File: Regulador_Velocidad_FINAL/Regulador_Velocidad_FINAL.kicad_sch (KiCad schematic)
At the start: 5 parts

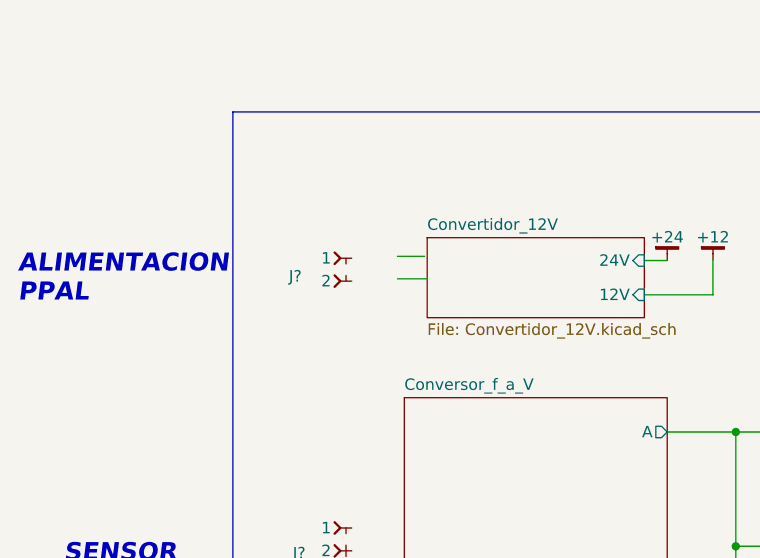
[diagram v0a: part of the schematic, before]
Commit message: Monitor_speed: Changes Schematics
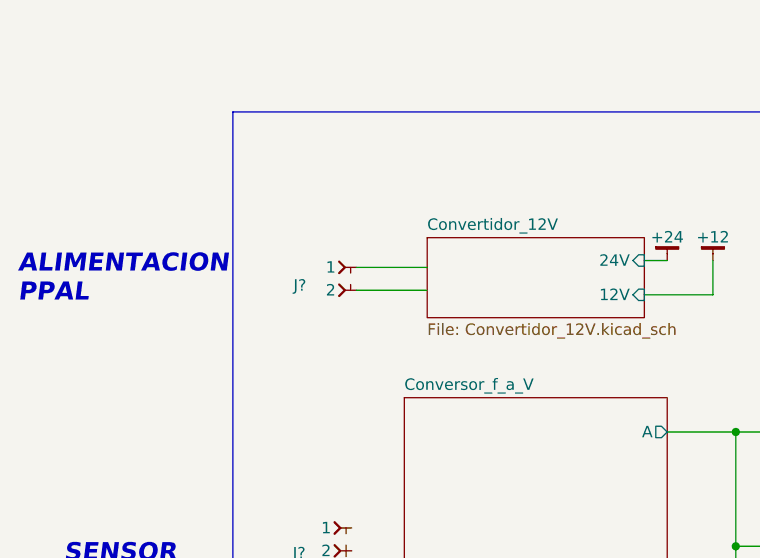
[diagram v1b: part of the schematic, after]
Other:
- moved on the sheet: J?
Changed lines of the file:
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@@
 (kicad_sch (version 20210621) (generator eeschema)
   (paper "A4")
+  (junction (at 149.098 100.33) (diameter 0) (color 0 0 0 0))
   (junction (at 149.098 113.03) (diameter 0) (color 0 0 0 0))
-  (junction (at 149.098 100.33) (diameter 0) (color 0 0 0 0))
   (wire (pts (xy 149.098 128.27) (xy 149.098 113.03))
     (stroke (width 0) (type default) (color 0 0 0 0))
   )
-  (wire (pts (xy 111.506 83.312) (xy 114.808 83.312))
-    (stroke (width 0) (type default) (color 0 0 0 0))
-  )
-  (wire (pts (xy 111.508 80.81) (xy 114.508 80.81))
+  (wire (pts (xy 106.934 84.582) (xy 114.808 84.582))
     (stroke (width 0) (type default) (color 0 0 0 0))
   )
@@
     (stroke (width 0) (type default) (color 0 0 0 0))
   )
+  (wire (pts (xy 146.558 85.09) (xy 146.558 81.28))
+    (stroke (width 0) (type default) (color 0 0 0 0))
+  )
   (wire (pts (xy 138.938 85.09) (xy 146.558 85.09))
     (stroke (width 0) (type default) (color 0 0 0 0))
   )
-  (wire (pts (xy 146.558 85.09) (xy 146.558 81.28))
+  (wire (pts (xy 106.934 82.042) (xy 114.808 82.042))
     (stroke (width 0) (type default) (color 0 0 0 0))
   )
@@
     (stroke (width 0) (type default) (color 0 0 0 0))
   )
+  (polyline (pts (xy 93.218 64.77) (xy 93.218 146.05))
+    (stroke (width 0) (type default) (color 0 0 0 0))
+  )
   (polyline (pts (xy 93.218 64.77) (xy 210.058 64.77))
     (stroke (width 0) (type default) (color 0 0 0 0))
   )
   (polyline (pts (xy 210.058 146.05) (xy 93.218 146.05))
-    (stroke (width 0) (type default) (color 0 0 0 0))
-  )
-  (polyline (pts (xy 93.218 64.77) (xy 93.218 146.05))
     (stroke (width 0) (type default) (color 0 0 0 0))
   )
@@
     (pin "3")
   )
-  (symbol (lib_id "conn-100mil:CONN-100MIL-F-1x2") (at 105.156 81.026 0) (mirror y) (unit 1)
-    (in_bom yes) (on_board yes)
-    (property "Reference" "J?" (id 0) (at 100.156 83.026 0))
-    (property "Value" "CONN-100MIL-F-1x2" (id 1) (at 105.0925 79.1996 0)
-      (effects (font (size 1.27 1.27)) hide)
-    )
-    (property "Footprint" "conn-100mil:CONN-100MIL-F-1x2" (id 2) (at 105.156 81.026 0)
-      (effects (font (size 1.27 1.27)) hide)
-    )
-    (property "Datasheet" "" (id 3) (at 105.156 81.026 0))
+  (symbol (lib_id "conn-100mil:CONN-100MIL-F-1x2") (at 105.664 82.042 0) (mirror y) (unit 1)
+    (in_bom yes) (on_board yes)
+    (property "Reference" "J?" (id 0) (at 100.664 84.042 0))
+    (property "Value" "CONN-100MIL-F-1x2" (id 1) (at 105.6005 80.2156 0)
+      (effects (font (size 1.27 1.27)) hide)
+    )
+    (property "Footprint" "conn-100mil:CONN-100MIL-F-1x2" (id 2) (at 105.664 82.042 0)
+      (effects (font (size 1.27 1.27)) hide)
+    )
+    (property "Datasheet" "" (id 3) (at 105.664 82.042 0))
     (pin "1")
     (pin "2")
@@
       (reference "#PWR?") (unit 1) (value "+24") (footprint "")
     )
+    (path "/00000000-0000-0000-0000-0000612e15a4/1888b6cc-01b4-4d63-b759-ff08c40e2ea5"
+      (reference "#PWR?") (unit 1) (value "+12") (footprint "")
+    )
     (path "/00000000-0000-0000-0000-0000612e15a4/191b58eb-f343-4e44-963c-006bd7e58632"
       (reference "#PWR?") (unit 1) (value "+12") (footprint "")
@@
       (reference "#PWR?") (unit 1) (value "GND") (footprint "")
     )
+    (path "/00000000-0000-0000-0000-0000612e15a4/bf605f14-3222-4811-bade-070d22a5da3e"
+      (reference "#PWR?") (unit 1) (value "+12") (footprint "")
+    )
     (path "/00000000-0000-0000-0000-0000612e3fd7/d6147ff6-8513-43f1-9dd7-b83e35a8992b"

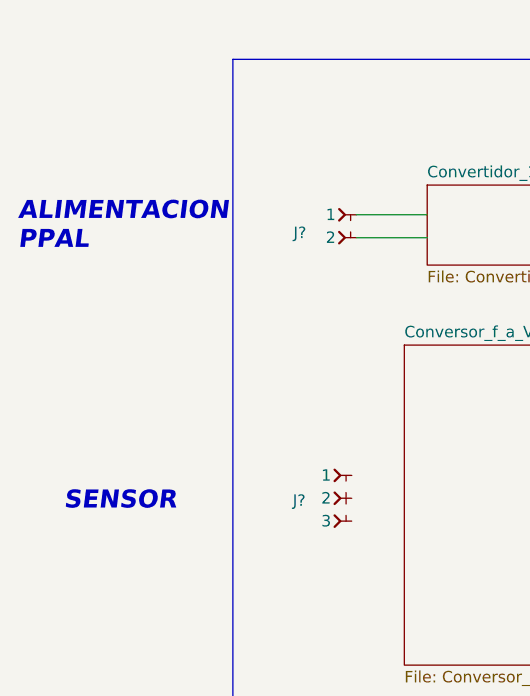
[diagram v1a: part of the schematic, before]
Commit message: Speed_Monitor: Changes on schematics
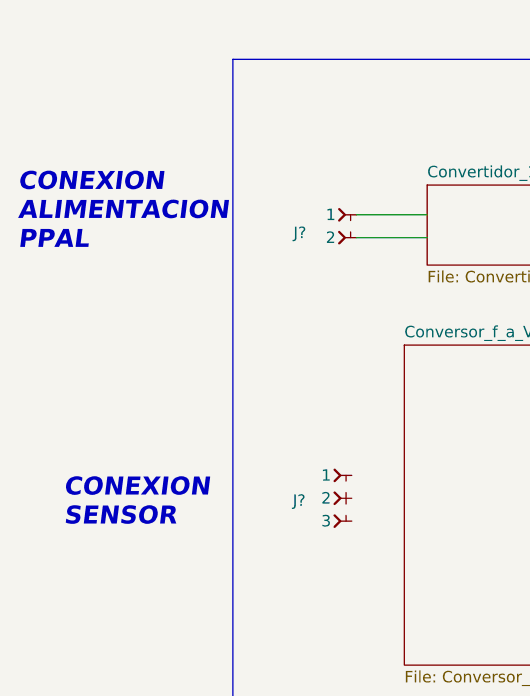
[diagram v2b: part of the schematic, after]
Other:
- note added: "CONEXION ALIMENTACION PPAL"
- note added: "CONEXION SENSOR"
- note removed: "ALIMENTACION PPAL"
- note removed: "SENSOR"
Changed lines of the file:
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@@
 (kicad_sch (version 20210621) (generator eeschema)
   (paper "A4")
+  (junction (at 149.098 113.03) (diameter 0) (color 0 0 0 0))
   (junction (at 149.098 100.33) (diameter 0) (color 0 0 0 0))
-  (junction (at 149.098 113.03) (diameter 0) (color 0 0 0 0))
   (wire (pts (xy 149.098 128.27) (xy 149.098 113.03))
     (stroke (width 0) (type default) (color 0 0 0 0))
@@
     (stroke (width 0) (type default) (color 0 0 0 0))
   )
+  (wire (pts (xy 138.938 85.09) (xy 146.558 85.09))
+    (stroke (width 0) (type default) (color 0 0 0 0))
+  )
   (wire (pts (xy 146.558 85.09) (xy 146.558 81.28))
     (stroke (width 0) (type default) (color 0 0 0 0))
   )
-  (wire (pts (xy 138.938 85.09) (xy 146.558 85.09))
-    (stroke (width 0) (type default) (color 0 0 0 0))
-  )
   (wire (pts (xy 106.934 82.042) (xy 114.808 82.042))
     (stroke (width 0) (type default) (color 0 0 0 0))
@@
     (stroke (width 0) (type default) (color 0 0 0 0))
   )
+  (polyline (pts (xy 210.058 146.05) (xy 93.218 146.05))
+    (stroke (width 0) (type default) (color 0 0 0 0))
+  )
+  (polyline (pts (xy 93.218 64.77) (xy 210.058 64.77))
+    (stroke (width 0) (type default) (color 0 0 0 0))
+  )
+  (polyline (pts (xy 210.058 64.77) (xy 210.058 146.05))
+    (stroke (width 0) (type default) (color 0 0 0 0))
+  )
   (polyline (pts (xy 93.218 64.77) (xy 93.218 146.05))
     (stroke (width 0) (type default) (color 0 0 0 0))
   )
-  (polyline (pts (xy 93.218 64.77) (xy 210.058 64.77))
-    (stroke (width 0) (type default) (color 0 0 0 0))
-  )
-  (polyline (pts (xy 210.058 146.05) (xy 93.218 146.05))
-    (stroke (width 0) (type default) (color 0 0 0 0))
-  )
-  (polyline (pts (xy 210.058 64.77) (xy 210.058 146.05))
-    (stroke (width 0) (type default) (color 0 0 0 0))
-  )
   (wire (pts (xy 138.938 81.28) (xy 141.478 81.28))
     (stroke (width 0) (type default) (color 0 0 0 0))
@@
     (effects (font (size 2 2) (thickness 0.4) bold italic) (justify left bottom))
   )
-  (text "SENSOR" (at 74.422 115.062 0)
-    (effects (font (size 2 2) (thickness 0.4) bold italic) (justify left bottom))
-  )
-  (text "ALIMENTACION\nPPAL" (at 69.342 86.106 0)
+  (text "CONEXION\nSENSOR" (at 74.422 116.84 0)
+    (effects (font (size 2 2) (thickness 0.4) bold italic) (justify left bottom))
+  )
+  (text "CONEXION\nALIMENTACION\nPPAL" (at 69.342 86.106 0)
     (effects (font (size 2 2) (thickness 0.4) bold italic) (justify left bottom))
   )
@@
       (reference "#PWR0105") (unit 1) (value "GND") (footprint "")
     )
-    (path "/00000000-0000-0000-0000-0000612e15a4/00000000-0000-0000-0000-00006131281b"
-      (reference "#PWR0106") (unit 1) (value "GND") (footprint "")
-    )
     (path "/00000000-0000-0000-0000-0000612e15a4/00000000-0000-0000-0000-000061312847"
       (reference "#PWR0107") (unit 1) (value "GND") (footprint "")
     )
-    (path "/00000000-0000-0000-0000-0000612e15a4/00000000-0000-0000-0000-000061312853"
-      (reference "#PWR0108") (unit 1) (value "GND") (footprint "")
-    )
     (path "/00000000-0000-0000-0000-0000612e15a4/00000000-0000-0000-0000-000061312865"
       (reference "#PWR0109") (unit 1) (value "GND") (footprint "")
@@
       (reference "#PWR?") (unit 1) (value "+12") (footprint "")
     )
+    (path "/00000000-0000-0000-0000-0000612e15a4/30ff6dd4-1562-413a-81cf-b765833a91db"
+      (reference "#PWR?") (unit 1) (value "+12") (footprint "")
+    )
     (path "/00000000-0000-0000-0000-000061322896/8bb79843-2e88-4533-bc74-6205b95b5360"
       (reference "#PWR?") (unit 1) (value "+24") (footprint "")
@@
       (reference "#PWR?") (unit 1) (value "GND") (footprint "")
     )
+    (path "/00000000-0000-0000-0000-0000612e15a4/b823652e-3346-4fc3-9ee0-0de81291789f"
+      (reference "#PWR?") (unit 1) (value "GND") (footprint "")
+    )
